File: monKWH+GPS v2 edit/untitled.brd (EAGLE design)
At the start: 77 x 60 mm, 67 parts, among them J1 U.FL-R-SMT(01), J2 DCJ0202, J3 2172034-1, J5 RJ45-8N-B, Q1 MMBT3904, Q2 MMBT3904, Q3 12MHz, U1 RT9193-33GB, U2 RT9193-33GB, U3 RT9193-33GB, U4 L80-R, U5 MAX232CSE, X1 MSTBA2

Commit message: Add files via upload
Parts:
- removed C28: 10uF/16V, rcl:153CLV-0505
- removed C29: 0.1uf/16V, rcl:153CLV-0505
- added C4: (no value), rcl:E2,5-7
- added U6: RA-01H, RA-01H:XCVR_RA-01H
- added X2: (no value), EYR_Conectores:5555164
- C13, C15, C16: value (none) -> 100nf
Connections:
- new net N$11: C4.+, PS1.3
- new net N$7: C4.-, PS1.4_1, PS1.4_2
- net 3V3-LAN-GPS: no longer C28.+, C29.+
- net 3V3-LORA-RS232: now also U6.3
- net ANT: now also U6.1
- net GND: now also U6.16, U6.2, U6.9; no longer C28.-, C29.-
- net LORA_DI0: now also U6.5
- net LORA_DI1: now also U6.6
- net MISO_VSPI: now also LORA-NICERF-V1.MISO, MD1.31, U6.13; no longer LORA-NICERF-V1.MOSI, MD1.37
- net MOSI_VSPI: now also LORA-NICERF-V1.MOSI, MD1.37, U6.14; no longer LORA-NICERF-V1.MISO, MD1.31
- net RST_LORA: now also U6.4
- net SCK_VSPI: now also U6.12
- net SS_LORA: now also U6.15
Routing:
- net GND: track 499.1 -> 453.6 mm, vias 100 -> 123
- net ANT: track 10.1 -> 42.6 mm, vias 1 -> 2
- net 3V3-LORA-RS232: track 132.3 -> 157.9 mm
- net 3V3-LAN-GPS: track 92.7 -> 81.5 mm
- net N$11: track 0.00 -> 7.14 mm
- net N$7: track 0.00 -> 7.08 mm
- net N$26: track 124.3 -> 118.7 mm
- net N$6: track 48.6 -> 53.4 mm
- net MOSI_VSPI: track 36.6 -> 41.2 mm
- net SS_LORA: track 35.6 -> 40.2 mm
- net MISO_VSPI: track 37.2 -> 41.4 mm
- net SCK_VSPI: track 36.3 -> 39.3 mm
- net N$16: track 39.9 -> 41.4 mm
- net RST_LORA: track 62.0 -> 62.7 mm

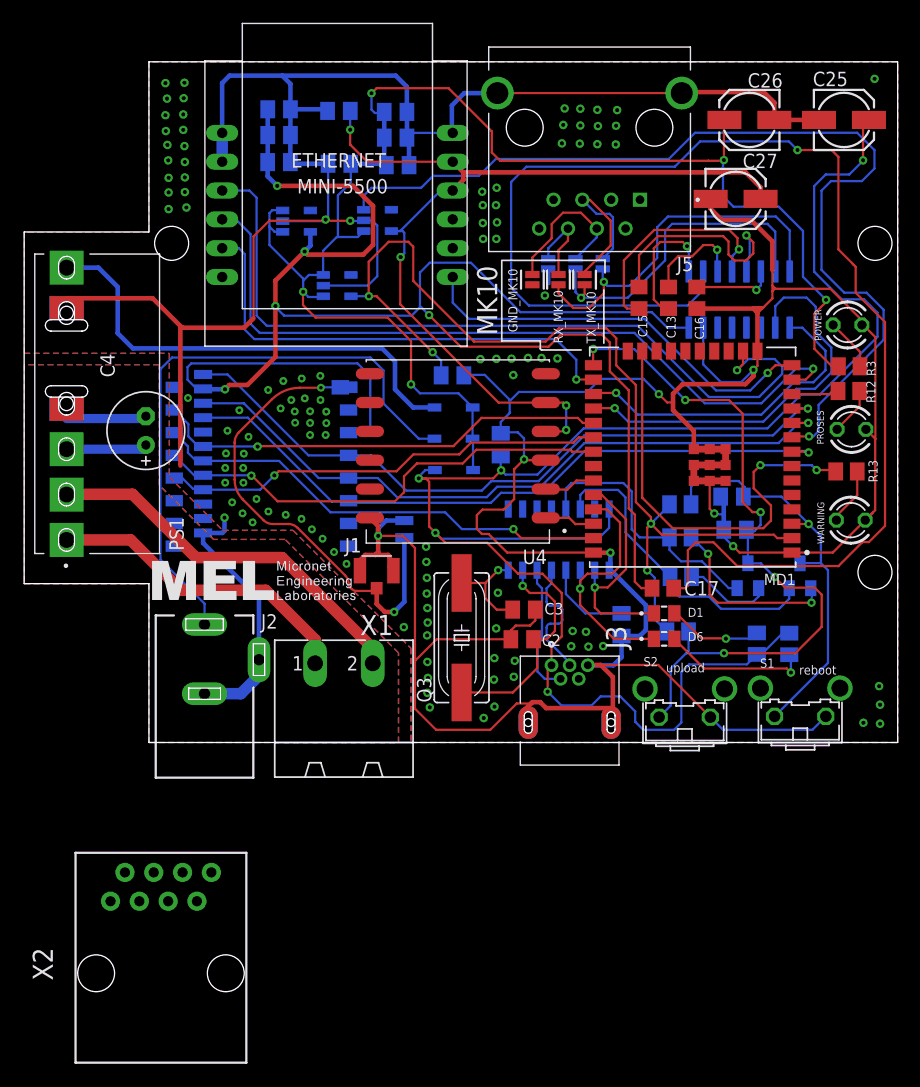
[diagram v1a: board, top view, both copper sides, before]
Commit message: change mini usb to micro usb
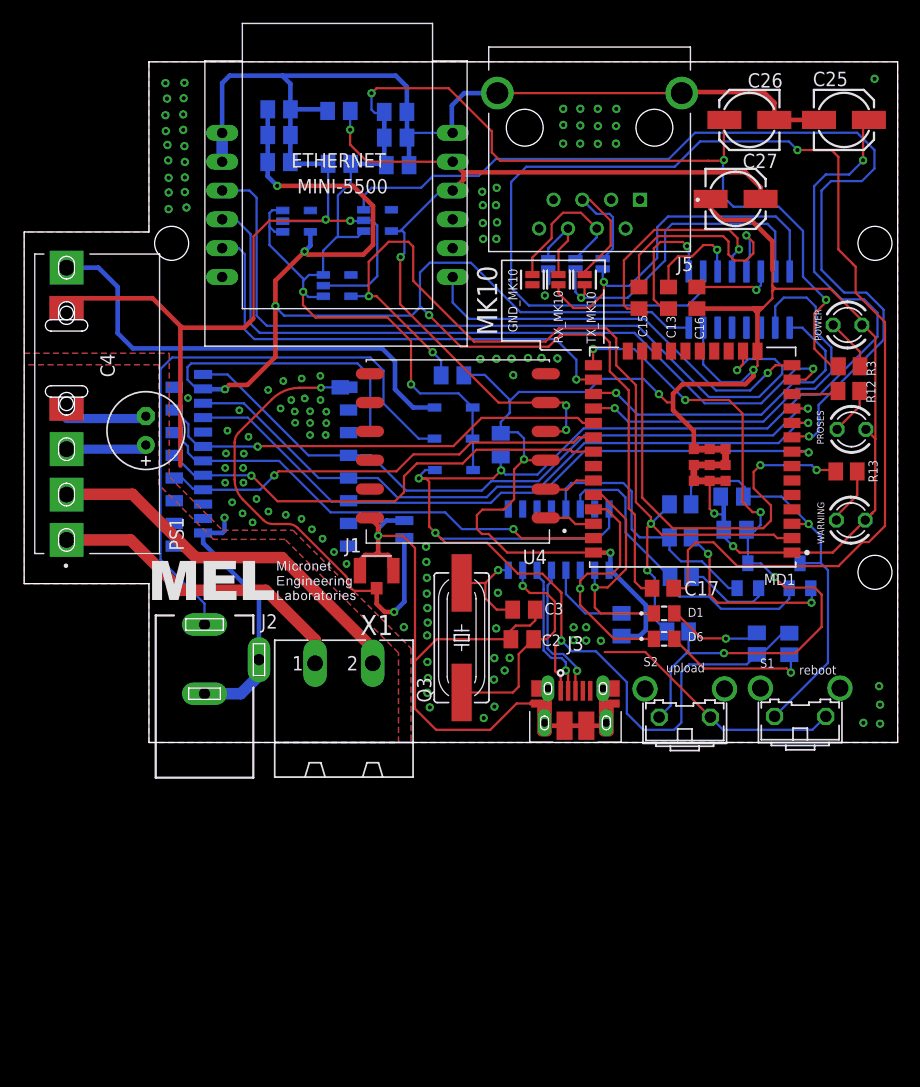
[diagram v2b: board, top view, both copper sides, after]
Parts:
- removed X2: (no value), EYR_Conectores:5555164
- C17: value (none) -> 1uF
- J3: value 2172034-1 -> 10103594; device 2172034-1:TE_2172034-1 -> Connector_USB:10103594
- moved J3 0.51 mm to (51.6, 41.7), turned to 0 degrees
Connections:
- net GND: now also J3.6, J3.7, J3.SH3, J3.SH4
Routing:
- net GND: track 453.6 -> 442.2 mm
- net VCC: track 150.7 -> 151.9 mm
- net USB_P: track 11.4 -> 12.4 mm, vias 0 -> 1
- net USB_N: track 11.6 -> 12.3 mm, vias 0 -> 1
